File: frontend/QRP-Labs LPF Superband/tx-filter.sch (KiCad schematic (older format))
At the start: 63 parts, among them K10 HK4100, K11 HK4100, K12 HK4100, K13 HK4100, K14 HK4100, K15 HK4100, K2 HK4100, K3 HK4100, K4 HK4100, K5 HK4100, K6 HK4100, K7 HK4100, K8 HK4100, K9 HK4100

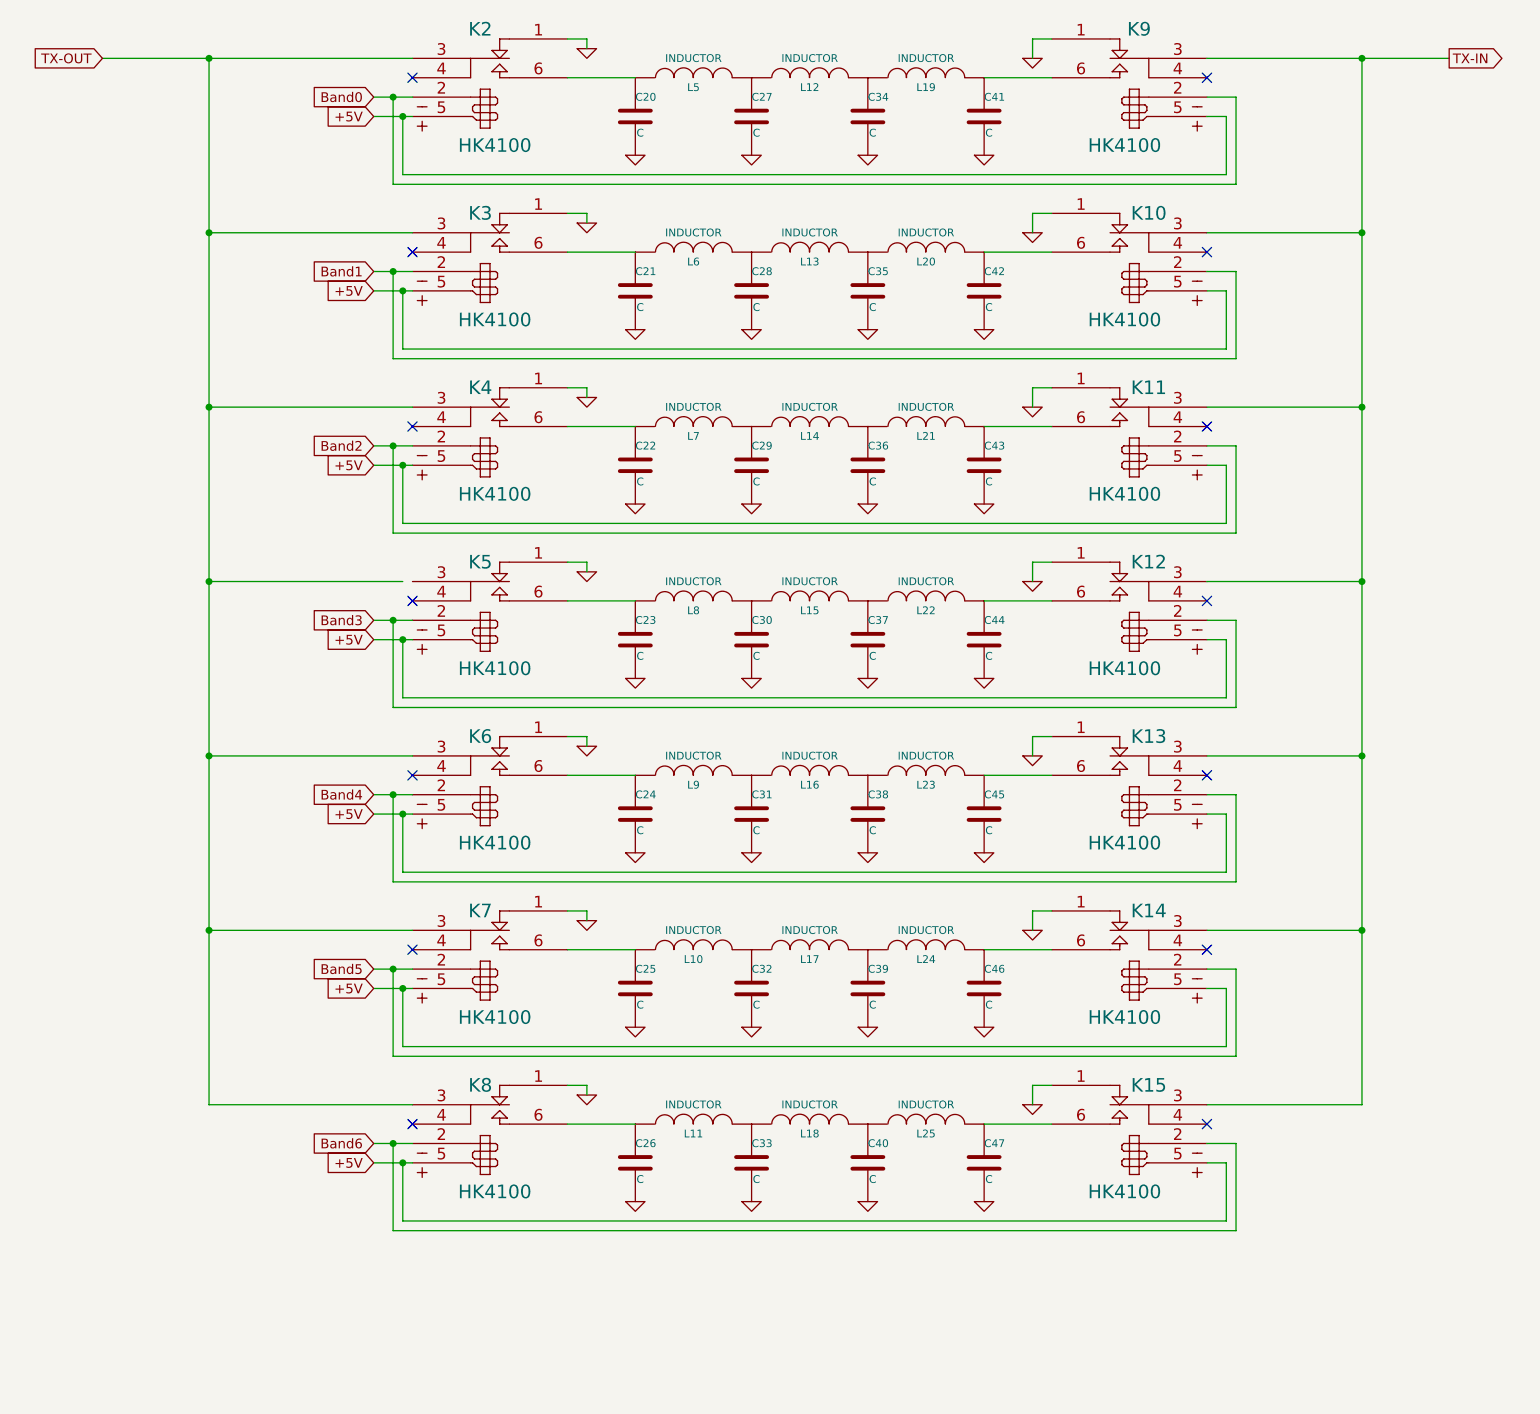
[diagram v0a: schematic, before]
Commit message: Further updates to the pre-V2 amp
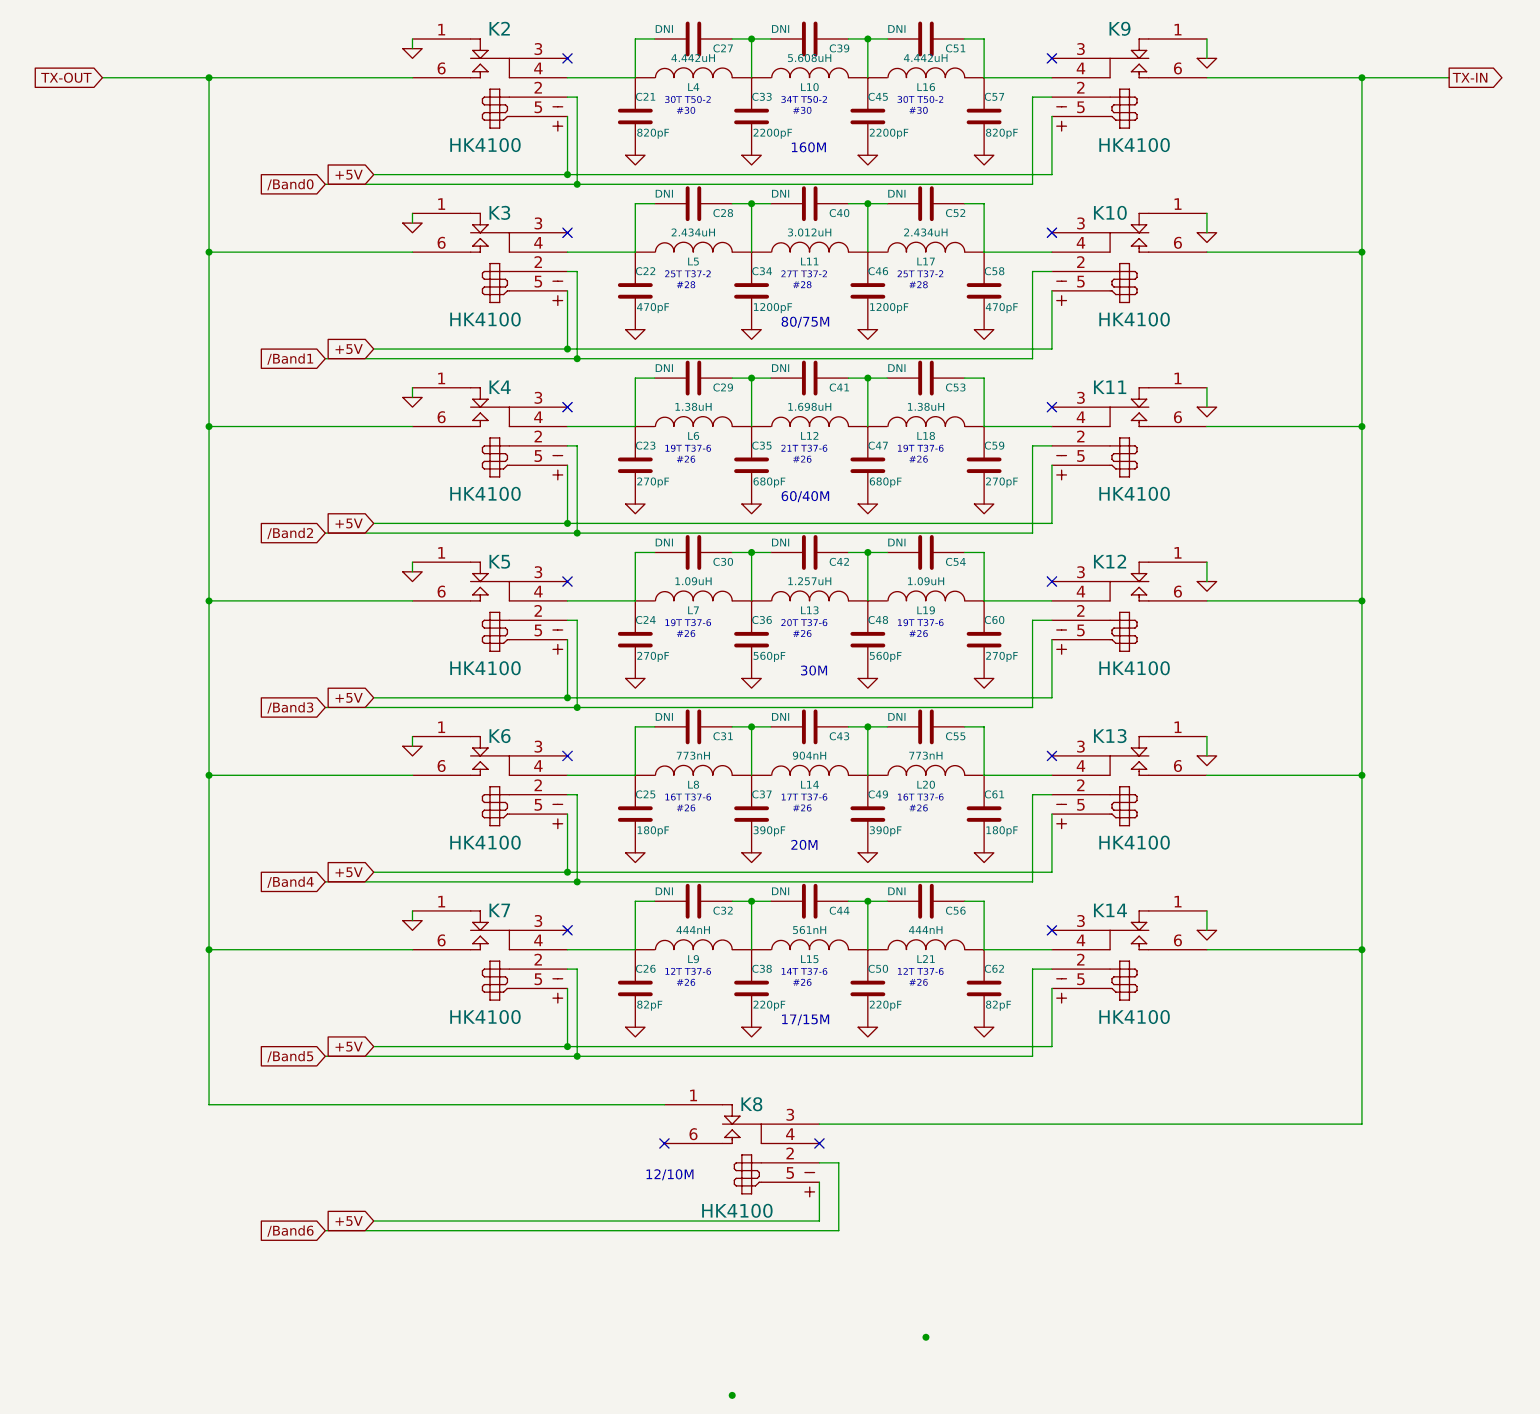
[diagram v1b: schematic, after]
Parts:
- removed C26, C33, C47: C, symbol C
- removed K15: HK4100, symbol HK4100
- removed L11, L18, L25: INDUCTOR, symbol INDUCTOR
- added C27, C28, C29, C30, C31, C32, C39, C41, C42, C43, C44, C51, C52, C53, C54, C55, C56: DNI, HERMESLITE:C_0805, symbol C
- C21: renamed from C20; value C -> 820pF; footprint (none) -> HERMESLITE:C_0805
- C22: renamed from C21; value C -> 470pF; footprint (none) -> HERMESLITE:C_0805
- C23: renamed from C22; value C -> 270pF; footprint (none) -> HERMESLITE:C_0805
- C24: renamed from C23; value C -> 270pF; footprint (none) -> HERMESLITE:C_0805
- C25: renamed from C24; value C -> 180pF; footprint (none) -> HERMESLITE:C_0805
- C26: renamed from C25; value C -> 82pF; footprint (none) -> HERMESLITE:C_0805
- C33: renamed from C27; value C -> 2200pF; footprint (none) -> HERMESLITE:C_0805
- C34: renamed from C28; value C -> 1200pF; footprint (none) -> HERMESLITE:C_0805
- C35: renamed from C29; value C -> 680pF; footprint (none) -> HERMESLITE:C_0805
- C36: renamed from C30; value C -> 560pF; footprint (none) -> HERMESLITE:C_0805
- C37: renamed from C31; value C -> 390pF; footprint (none) -> HERMESLITE:C_0805
- C38: renamed from C32; value C -> 220pF; footprint (none) -> HERMESLITE:C_0805
- C40: value C -> DNI; footprint (none) -> HERMESLITE:C_0805
- C45: renamed from C34; value C -> 2200pF; footprint (none) -> HERMESLITE:C_0805
- C46: renamed from C35; value C -> 1200pF; footprint (none) -> HERMESLITE:C_0805
- C47: renamed from C36; value C -> 680pF; footprint (none) -> HERMESLITE:C_0805
- C48: renamed from C37; value C -> 560pF; footprint (none) -> HERMESLITE:C_0805
- C49: renamed from C38; value C -> 390pF; footprint (none) -> HERMESLITE:C_0805
- C50: renamed from C39; value C -> 220pF; footprint (none) -> HERMESLITE:C_0805
- C57: renamed from C41; value C -> 820pF; footprint (none) -> HERMESLITE:C_0805
- C58: renamed from C42; value C -> 470pF; footprint (none) -> HERMESLITE:C_0805
- C59: renamed from C43; value C -> 270pF; footprint (none) -> HERMESLITE:C_0805
- C60: renamed from C44; value C -> 270pF; footprint (none) -> HERMESLITE:C_0805
- C61: renamed from C45; value C -> 180pF; footprint (none) -> HERMESLITE:C_0805
- C62: renamed from C46; value C -> 82pF; footprint (none) -> HERMESLITE:C_0805
- K10, K11, K12, K13, K14, K2, K3, K4, K5, K6, K7, K8, K9: footprint (none) -> HERMESLITE:HK4100
- L10: renamed from L12; value INDUCTOR -> 5.608uH; footprint (none) -> Choke_Toroid_ThroughHole:Choke_Toroid_5x10mm_Vertical
- L11: renamed from L13; value INDUCTOR -> 3.012uH; footprint (none) -> Choke_Toroid_ThroughHole:Choke_Toroid_5x10mm_Vertical
- L12: renamed from L14; value INDUCTOR -> 1.698uH; footprint (none) -> Choke_Toroid_ThroughHole:Choke_Toroid_5x10mm_Vertical
- L13: renamed from L15; value INDUCTOR -> 1.257uH; footprint (none) -> Choke_Toroid_ThroughHole:Choke_Toroid_5x10mm_Vertical
- L14: renamed from L16; value INDUCTOR -> 904nH; footprint (none) -> Choke_Toroid_ThroughHole:Choke_Toroid_5x10mm_Vertical
- L15: renamed from L17; value INDUCTOR -> 561nH; footprint (none) -> Choke_Toroid_ThroughHole:Choke_Toroid_5x10mm_Vertical
- L16: renamed from L19; value INDUCTOR -> 4.442uH; footprint (none) -> Choke_Toroid_ThroughHole:Choke_Toroid_5x10mm_Vertical
- L17: renamed from L20; value INDUCTOR -> 2.434uH; footprint (none) -> Choke_Toroid_ThroughHole:Choke_Toroid_5x10mm_Vertical
- L18: renamed from L21; value INDUCTOR -> 1.38uH; footprint (none) -> Choke_Toroid_ThroughHole:Choke_Toroid_5x10mm_Vertical
- L19: renamed from L22; value INDUCTOR -> 1.09uH; footprint (none) -> Choke_Toroid_ThroughHole:Choke_Toroid_5x10mm_Vertical
- L20: renamed from L23; value INDUCTOR -> 773nH; footprint (none) -> Choke_Toroid_ThroughHole:Choke_Toroid_5x10mm_Vertical
- L21: renamed from L24; value INDUCTOR -> 444nH; footprint (none) -> Choke_Toroid_ThroughHole:Choke_Toroid_5x10mm_Vertical
- L4: renamed from L5; value INDUCTOR -> 4.442uH; footprint (none) -> Choke_Toroid_ThroughHole:Choke_Toroid_6,5x13mm_Vertical
- L5: renamed from L6; value INDUCTOR -> 2.434uH; footprint (none) -> Choke_Toroid_ThroughHole:Choke_Toroid_5x10mm_Vertical
- L6: renamed from L7; value INDUCTOR -> 1.38uH; footprint (none) -> Choke_Toroid_ThroughHole:Choke_Toroid_5x10mm_Vertical
- L7: renamed from L8; value INDUCTOR -> 1.09uH; footprint (none) -> Choke_Toroid_ThroughHole:Choke_Toroid_5x10mm_Vertical
- L8: renamed from L9; value INDUCTOR -> 773nH; footprint (none) -> Choke_Toroid_ThroughHole:Choke_Toroid_5x10mm_Vertical
- L9: renamed from L10; value INDUCTOR -> 444nH; footprint (none) -> Choke_Toroid_ThroughHole:Choke_Toroid_5x10mm_Vertical
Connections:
- net GND: no longer C40.2, K8.1
- net TX-IN: now also K10.6, K11.6, K12.6, K13.6, K14.6, K8.3, K9.6; no longer K10.3, K11.3, K12.3, K13.3, K14.3, K9.3
- net TX-OUT: now also K2.6, K3.6, K4.6, K5.6, K6.6, K7.6, K8.1; no longer K2.3, K3.3, K4.3, K6.3, K7.3, K8.3
- net at C21.1, L4.1: now also K2.4, C27.2; no longer K2.6
- net at C33.1, L10.1, L4.2: now also C27.1, C39.2
- net at C45.1, L10.2, L16.1: now also C39.1, C51.2
- net at C57.1, L16.2: now also K9.4, C51.1; no longer K9.6
- net at C22.1, L5.1: now also K3.4, C28.2; no longer K3.6
- net at C34.1, L11.1, L5.2: now also C40.2, C28.1
- net at C46.1, L11.2, L17.1: now also C40.1, C52.2
- net at C58.1, L17.2: now also K10.4, C52.1; no longer K10.6
- net at C23.1, L6.1: now also K4.4, C29.2; no longer K4.6
- net at C35.1, L12.1, L6.2: now also C29.1, C41.2
- net at C47.1, L12.2, L18.1: now also C41.1, C53.2
- net at C59.1, L18.2: now also K11.4, C53.1; no longer K11.6
- net at C24.1, L7.1: now also K5.4, C30.2; no longer K5.6
- net at C36.1, L13.1, L7.2: now also C30.1, C42.2
- net at C48.1, L13.2, L19.1: now also C42.1, C54.2
- net at C60.1, L19.2: now also K12.4, C54.1; no longer K12.6
- net at C25.1, L8.1: now also K6.4, C31.2; no longer K6.6
- net at C37.1, L14.1, L8.2: now also C31.1, C43.2
- net at C49.1, L14.2, L20.1: now also C43.1, C55.2
- net at C61.1, L20.2: now also K13.4, C55.1; no longer K13.6
- net at C26.1, L9.1: now also K7.4, C32.2; no longer K7.6
- net at C38.1, L15.1, L9.2: now also C32.1, C44.2
- net at C50.1, L15.2, L21.1: now also C44.1, C56.2
- net at C62.1, L21.2: now also K14.4, C56.1; no longer K14.6
- net Band0 renamed /Band0
- net Band1 renamed /Band1
- net Band2 renamed /Band2
- net Band3 renamed /Band3
- net Band4 renamed /Band4
- net Band5 renamed /Band5
- net Band6 renamed /Band6
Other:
- note added: "12/10M"
- note added: "12T T37-6\n #26"
- note added: "14T T37-6\n #26"
- note added: "160M"
- note added: "16T T37-6\n #26"
- note added: "17/15M"
- note added: "17T T37-6\n #26"
- note added: "19T T37-6\n #26"
- note added: "20M"
- note added: "20T T37-6\n #26"
- note added: "21T T37-6\n #26"
- note added: "25T T37-2 \n #28"
- note added: "27T T37-2 \n #28"
- note added: "30M"
- note added: "30T T50-2 \n #30"
- note added: "34T T50-2 \n #30"
- note added: "60/40M"
- note added: "80/75M"
